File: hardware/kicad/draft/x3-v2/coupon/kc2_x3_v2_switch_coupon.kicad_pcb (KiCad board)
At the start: 2 copper layers, 64 x 32 mm, 6 parts

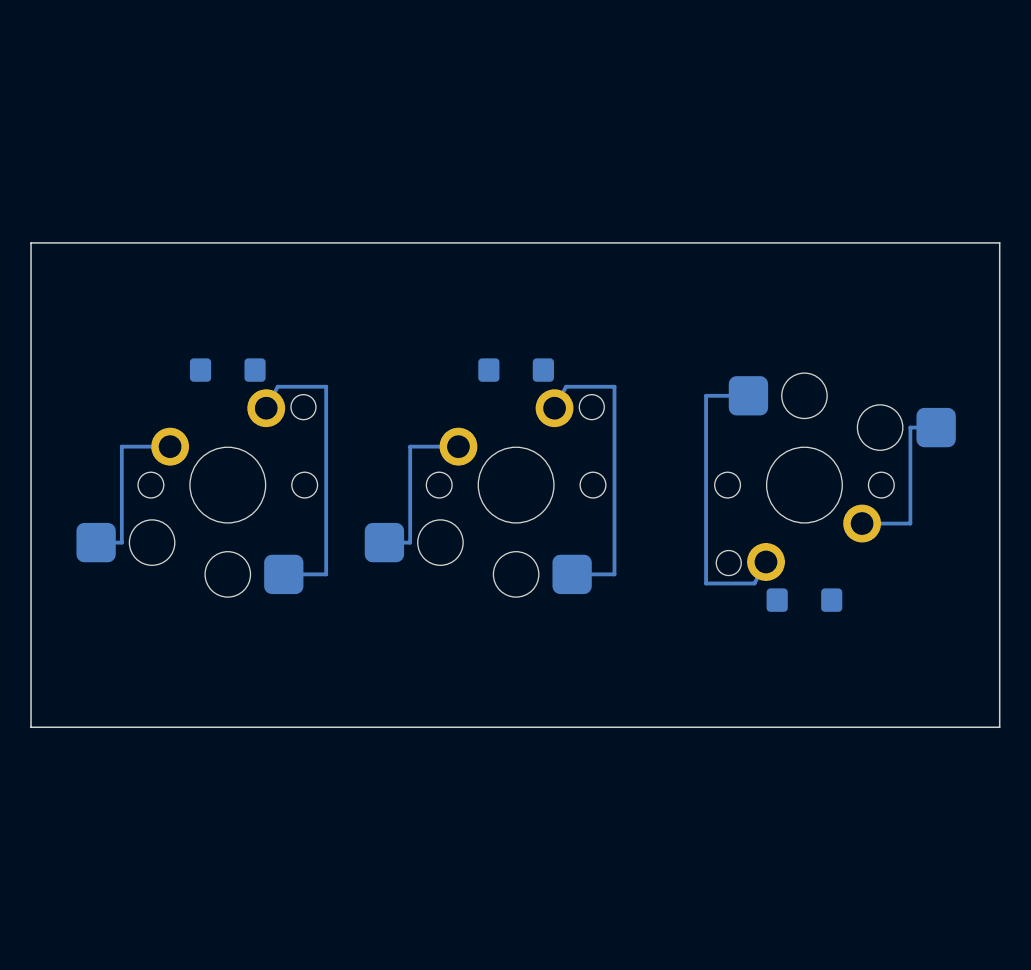
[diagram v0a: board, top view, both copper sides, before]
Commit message: feat(x3-v2): finalize ES1B mounting prototype
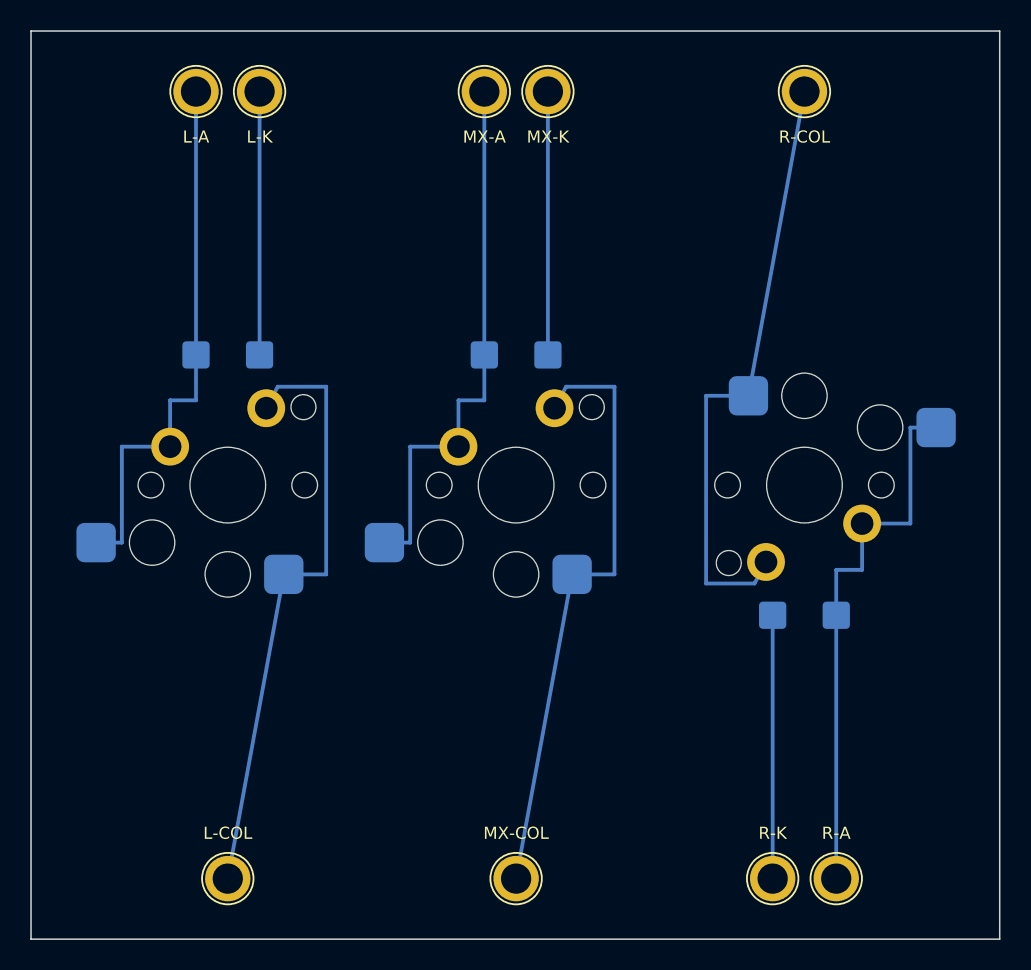
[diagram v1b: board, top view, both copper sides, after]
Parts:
- removed the D_L at (28.0, 32.4)
- removed the D_MX at (47.0, 32.4)
- removed the D_R at (66.1, 47.6)
- added D_L: ES1B_Jingdao_C437840_Eleparts9475342, D_ES1B_SMA_HandSolder_C437840, B.Cu at (28.0, 31.4)
- added D_MX: ES1B_Jingdao_C437840_Eleparts9475342, D_ES1B_SMA_HandSolder_C437840, B.Cu at (47.0, 31.4)
- added D_R: ES1B_Jingdao_C437840_Eleparts9475342, D_ES1B_SMA_HandSolder_C437840, B.Cu at (66.1, 48.6)
- added TP_L_ANODE: 2.0mm_PTH_SERVICE_PROBE, TestPoint_Plated_Hole_D2.0mm, F.Cu at (25.9, 14.0)
- added TP_L_COL: 2.0mm_PTH_SERVICE_PROBE, TestPoint_Plated_Hole_D2.0mm, F.Cu at (28.0, 66.0)
- added TP_L_ROW: 2.0mm_PTH_SERVICE_PROBE, TestPoint_Plated_Hole_D2.0mm, F.Cu at (30.1, 14.0)
- added TP_MX_ANODE: 2.0mm_PTH_SERVICE_PROBE, TestPoint_Plated_Hole_D2.0mm, F.Cu at (45.0, 14.0)
- added TP_MX_COL: 2.0mm_PTH_SERVICE_PROBE, TestPoint_Plated_Hole_D2.0mm, F.Cu at (47.0, 66.0)
- added TP_MX_ROW: 2.0mm_PTH_SERVICE_PROBE, TestPoint_Plated_Hole_D2.0mm, F.Cu at (49.1, 14.0)
- added TP_R_ANODE: 2.0mm_PTH_SERVICE_PROBE, TestPoint_Plated_Hole_D2.0mm, F.Cu at (68.2, 66.0)
- added TP_R_COL: 2.0mm_PTH_SERVICE_PROBE, TestPoint_Plated_Hole_D2.0mm, F.Cu at (66.1, 14.0)
- added TP_R_ROW: 2.0mm_PTH_SERVICE_PROBE, TestPoint_Plated_Hole_D2.0mm, F.Cu at (64.0, 66.0)
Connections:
- SW_L pad 1: SW_L_CONTACT_1 -> D_L_COL
- SW_L pad 2: SW_L_CONTACT_2 -> D_L_ANODE
- SW_MX pad 1: SW_MX_CONTACT_1 -> D_MX_COL
- SW_MX pad 2: SW_MX_CONTACT_2 -> D_MX_ANODE
- SW_R pad 1: SW_R_CONTACT_1 -> D_R_COL
- SW_R pad 2: SW_R_CONTACT_2 -> D_R_ANODE
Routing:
- net D_R_COL: track 0.00 -> 40.4 mm
- net D_MX_COL: track 0.00 -> 40.4 mm
- net D_L_COL: track 0.00 -> 40.4 mm
- net D_MX_ANODE: track 0.00 -> 36.4 mm
- net D_R_ANODE: track 0.00 -> 36.4 mm
- net D_L_ANODE: track 0.00 -> 36.4 mm
- net SW_R_CONTACT_1: track 20.0 -> 0.00 mm
- net SW_MX_CONTACT_1: track 20.0 -> 0.00 mm
- net SW_L_CONTACT_1: track 20.0 -> 0.00 mm
- net D_R_ROW: track 0.00 -> 17.4 mm
- net D_MX_ROW: track 0.00 -> 17.4 mm
- net D_L_ROW: track 0.00 -> 17.4 mm
- net SW_R_CONTACT_2: track 11.2 -> 0.00 mm
- net SW_MX_CONTACT_2: track 11.2 -> 0.00 mm
- net SW_L_CONTACT_2: track 11.2 -> 0.00 mm
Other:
- board size 64 x 32 mm -> 64 x 60 mm
- board text added: "D_L A/P2 SWITCH"
- board text added: "D_L K/P1 ROW"
- board text added: "D_MX A/P2 SWITCH"
- board text added: "D_MX K/P1 ROW"
- board text added: "D_R A/P2 SWITCH"
- board text added: "D_R K/P1 ROW"
- board text added: "ES1B C437840: K/P1=ROW A/P2=SWITCH"
- board text added: "L-A"
- board text added: "L-COL"
- board text added: "L-K"
- board text added: "MX-A"
- board text added: "MX-COL"
- board text added: "MX-K"
- board text added: "PHYSICAL VF / ROW-HIGH / ZERO-WAIT TEST PENDING"
- board text added: "R-A"
- board text added: "R-COL"
- board text added: "R-K"

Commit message: feat(x3-v2): adopt 1N4148W and dense housing supports
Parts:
- removed the D_L at (28.0, 31.4)
- removed the D_MX at (47.0, 31.4)
- removed the D_R at (66.1, 48.6)
- added D_L: 1N4148W-13-F_DiodesInc_SOD123, D_1N4148W_SOD123_HandSolder_DiodesInc, B.Cu at (28.0, 31.4)
- added D_MX: 1N4148W-13-F_DiodesInc_SOD123, D_1N4148W_SOD123_HandSolder_DiodesInc, B.Cu at (47.0, 31.4)
- added D_R: 1N4148W-13-F_DiodesInc_SOD123, D_1N4148W_SOD123_HandSolder_DiodesInc, B.Cu at (66.1, 48.6)
- moved TP_R_ANODE 0.30 mm to (67.9, 66.0)
- moved TP_L_ANODE 0.30 mm to (26.2, 14.0)
- moved TP_L_ROW 0.30 mm to (29.8, 14.0)
- moved TP_MX_ANODE 0.30 mm to (45.2, 14.0)
- moved TP_MX_ROW 0.30 mm to (48.9, 14.0)
- moved TP_R_ROW 0.30 mm to (64.3, 66.0)
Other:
- board text added: "1N4148W-13-F SOD-123: K/P1=ROW A/P2=SWITCH"
- board text removed: "ES1B C437840: K/P1=ROW A/P2=SWITCH"
